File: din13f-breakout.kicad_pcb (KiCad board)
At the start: 2 copper layers, 37.8 x 42.7 mm, 5 parts, among them J1 DB15_Female_HighDensity, J2 RCJ-017, J3 Conn_01x13, J4 SDD-130J

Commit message: WIP for op-amps
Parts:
- removed J2: RCJ-017, Jacks:CUI_RCJ-017
- removed J3: Conn_01x13, Connectors:13p_GrabPads
- removed TP1: TestPoint, TestPoint:TestPoint_Pad_2.5x2.5mm
- added C1: 0.1µF, Capacitor_SMD:C_0805_2012Metric_Pad1.18x1.45mm_HandSolder, F.Cu at (163.1, 58.8)
- added C2: 0.1µF, Capacitor_SMD:C_0805_2012Metric_Pad1.18x1.45mm_HandSolder, F.Cu at (163.1, 61.8)
- added C3: 0.1µF, Capacitor_SMD:C_0805_2012Metric_Pad1.18x1.45mm_HandSolder, F.Cu at (163.1, 64.8)
- added C4: 220µF, Capacitor_THT:CP_Radial_D8.0mm_P3.50mm, F.Cu at (154.2, 62.0)
- added D1: LED, LED_THT:LED_D3.0mm, F.Cu at (119.8, 64.2)
- added JP1: Jumper_2_Open, Resistor_SMD:R_0805_2012Metric_Pad1.20x1.40mm_HandSolder, F.Cu at (170.4, 40.7)
- added JP2: Jumper_2_Bridged, Jumper:SolderJumper-2_P1.3mm_Bridged_RoundedPad1.0x1.5mm, F.Cu at (170.2, 55.7)
- added JP3: Jumper_2_Bridged, Jumper:SolderJumper-2_P1.3mm_Bridged_RoundedPad1.0x1.5mm, F.Cu at (170.2, 59.3)
- added JP4: Jumper_2_Bridged, Jumper:SolderJumper-2_P1.3mm_Bridged_RoundedPad1.0x1.5mm, F.Cu at (170.2, 62.8)
- added R1: 680kΩ, Resistor_SMD:R_0805_2012Metric_Pad1.20x1.40mm_HandSolder, F.Cu at (170.4, 43.6)
- added R10: 4.3kΩ, Resistor_SMD:R_0805_2012Metric_Pad1.20x1.40mm_HandSolder, F.Cu at (179.9, 40.7)
- added R11: 4.3kΩ, Resistor_SMD:R_0805_2012Metric_Pad1.20x1.40mm_HandSolder, F.Cu at (179.9, 43.6)
- added R12: 4.3kΩ, Resistor_SMD:R_0805_2012Metric_Pad1.20x1.40mm_HandSolder, F.Cu at (179.9, 46.6)
- added R2: 330Ω, Resistor_SMD:R_0805_2012Metric_Pad1.20x1.40mm_HandSolder, F.Cu at (170.4, 46.6)
- added R3: 330Ω, Resistor_SMD:R_0805_2012Metric_Pad1.20x1.40mm_HandSolder, F.Cu at (170.4, 49.5)
- added R4: 560Ω, Resistor_SMD:R_0805_2012Metric_Pad1.20x1.40mm_HandSolder, F.Cu at (170.4, 52.5)
- added R5: 1kΩ, Resistor_SMD:R_0805_2012Metric_Pad1.20x1.40mm_HandSolder, F.Cu at (175.1, 40.7)
- added R6: 1kΩ, Resistor_SMD:R_0805_2012Metric_Pad1.20x1.40mm_HandSolder, F.Cu at (175.1, 43.6)
- added R7: 10kΩ, Resistor_SMD:R_0805_2012Metric_Pad1.20x1.40mm_HandSolder, F.Cu at (175.1, 46.6)
- added R8: 10kΩ, Resistor_SMD:R_0805_2012Metric_Pad1.20x1.40mm_HandSolder, F.Cu at (175.1, 49.5)
- added R9: 10kΩ, Resistor_SMD:R_0805_2012Metric_Pad1.20x1.40mm_HandSolder, F.Cu at (175.1, 52.5)
- added U1: LM1881, Package_SO:SOIC-8_3.9x4.9mm_P1.27mm, F.Cu at (160.1, 123.2)
- added U2: 74LS00, Package_DIP:DIP-14_W7.62mm_Socket_LongPads, F.Cu at (159.4, 115.6)
- added U3: ~, Package_SO:SOIC-14_3.9x8.7mm_P1.27mm, F.Cu at (149.9, 111.8)
- added X1: USB-B1HSB6, USB-B1HSB6:OST_USB-B1HSB6, F.Cu at (189.9, 100.2)
- J1: value DB15_Female_HighDensity -> SCART-F; footprint Connector_TE_AMP_HD15:FIXED-1-1734530-1 -> ninigi-scart-ra:NINIGI-SCART-RA
- moved J4 67.6 mm to (197.3, 120.1), turned to 90 degrees
- moved J1 40.2 mm to (131.7, 111.9), turned to -90 degrees
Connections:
- J1 pad 1: /RED -> unconnected-(J1-P1-Pad1)
- J1 pad 10: /VGND -> unconnected-(J1-P10-Pad10)
- J1 pad 11: unconnected-(J1-Pad11) -> /SCART_Green
- J1 pad 13: /HSYNC -> GND
- J1 pad 14: /VSYNC -> unconnected-(J1-P14-Pad14)
- J1 pad 15: unconnected-(J1-Pad15) -> /SCART_Red
- J1 pad 16: (no net) -> /Blanking
- J1 pad 17: (no net) -> GND
- J1 pad 2: /GREEN -> Net-(J1-P2)
- J1 pad 3: /BLUE -> unconnected-(J1-P3-Pad3)
- J1 pad 4: unconnected-(J1-Pad4) -> GND
- J1 pad 5: /VGND -> GND
- J1 pad 6: /VGND -> Net-(J1-P6)
- J1 pad 7: /VGND -> /SCART_Blue
- J1 pad 8: /VGND -> /AV_Control
- J1 pad 9: unconnected-(J1-Pad9) -> GND
- J4 pad 12: /VSYNC -> /VSync
- J4 pad 13: /VGND -> GND
- J4 pad 2: /CVID -> Net-(JP1-B)
- J4 pad 4: /~{MONO} -> /~{MONO_EN}
- J4 pad 5: /AUDIO_IN -> unconnected-(J4-Pad5)
- J4 pad 9: /HSYNC -> /HSync
- J4 pad E1: Net-(J4-PadE1) -> GND
- J4 pad E2: Net-(J4-PadE1) -> GND
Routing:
- net /CVID: track 63.4 -> 0.00 mm, vias 2 -> 0
- net /VGND: track 59.5 -> 0.00 mm
- net /VSYNC: track 48.9 -> 0.00 mm
- net /HSYNC: track 48.4 -> 0.00 mm, vias 2 -> 0
- net /AUDIO_OUT: track 45.7 -> 0.00 mm, vias 2 -> 0
- net /BLUE: track 38.0 -> 0.00 mm, vias 2 -> 0
- net /AUDIO_IN: track 36.4 -> 0.00 mm, vias 2 -> 0
- net /GREEN: track 31.9 -> 0.00 mm, vias 1 -> 0
- net /RED: track 29.8 -> 0.00 mm, vias 1 -> 0
- net /GPO: track 28.8 -> 0.00 mm, vias 2 -> 0
- net /~{MONO}: track 27.1 -> 0.00 mm, vias 2 -> 0
- net Net-(J4-PadE1): track 19.3 -> 0.00 mm, vias 1 -> 0
- net /+12V: track 17.0 -> 0.00 mm, vias 2 -> 0
- net /MONOVID: track 12.1 -> 0.00 mm, vias 1 -> 0
- removed copper zone on B.Cu, net /VGND
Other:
- board outline removed
- board text removed: "+12V"
- board text removed: "1"
- board text removed: "13"
- board text removed: "2022, v0.1"
- board text removed: "Aud. In"
- board text removed: "Aud. Out"
- board text removed: "B"
- board text removed: "Blue"
- board text removed: "C.Video"
- board text removed: "G"
- board text removed: "GPO"
- board text removed: "Green"
- board text removed: "HS"
- board text removed: "HSync"
- board text removed: "Mono Video"
- board text removed: "R"
- board text removed: "Red"
- board text removed: "Shield GND"
- board text removed: "TE 1-1734530-1"
- board text removed: "VGA"
- board text removed: "VS"
- board text removed: "VSync"
- board text removed: "leadedsolder.com"
- board text removed: "st monitor 13-pin DIN breakout"
- board text removed: "~{MONO}"

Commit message: No more DIP
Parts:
- added C5: 0.1µF, Capacitor_SMD:C_0805_2012Metric_Pad1.18x1.45mm_HandSolder, F.Cu at (139.9, 64.1)
- U2: footprint Package_DIP:DIP-14_W7.62mm_Socket_LongPads -> Package_SO:SOIC-14_3.9x8.7mm_P1.27mm
- U3: value ~ -> MCP6499
- moved U3 10.3 mm to (140.4, 108.0)
- moved U2 2.60 mm to (160.0, 113.0), turned to 0 degrees

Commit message: Laying out the birdseed
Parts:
- moved R3 88.5 mm to (143.9, 134.0)
- moved R2 88.3 mm to (143.8, 130.8)
- moved R1 81.1 mm to (172.1, 124.7), turned to -90 degrees
- moved R11 80.0 mm to (144.3, 115.3)
- moved JP1 79.0 mm to (177.4, 119.4)
- moved JP3 77.8 mm to (139.7, 130.8)
- moved JP4 77.4 mm to (139.7, 134.0)
- moved R8 73.8 mm to (139.7, 114.3), turned to 90 degrees
- moved R12 70.3 mm to (152.4, 111.3)
- moved JP2 70.0 mm to (149.2, 122.6)
- moved R6 70.0 mm to (145.8, 107.2), turned to -90 degrees
- moved R10 68.3 mm to (152.4, 103.1)
- moved R5 67.0 mm to (157.0, 105.1), turned to -90 degrees
- moved R9 65.8 mm to (147.8, 112.3), turned to 90 degrees
- moved C1 64.5 mm to (153.4, 122.6)
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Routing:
- net Net-(U1-VIDEO): track 0.00 -> 3.14 mm
- net /SCART_CSYNC: track 0.00 -> 2.54 mm

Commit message: Fully popped
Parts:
- added REF**: MountingHole_3.2mm_M3_DIN965_Pad, MountingHole:MountingHole_3.2mm_M3_DIN965_Pad, F.Cu at (151.8, 90.2)
- added REF**: MountingHole_3.2mm_M3_DIN965_Pad, MountingHole:MountingHole_3.2mm_M3_DIN965_Pad, F.Cu at (193.7, 90.2)
- added REF**: MountingHole_3.2mm_M3_DIN965_Pad, MountingHole:MountingHole_3.2mm_M3_DIN965_Pad, F.Cu at (151.8, 133.3)
- added REF**: MountingHole_3.2mm_M3_DIN965_Pad, MountingHole:MountingHole_3.2mm_M3_DIN965_Pad, F.Cu at (193.7, 133.3)
- added TP1: TestPoint, TestPoint:TestPoint_Loop_D2.50mm_Drill1.0mm, F.Cu at (176.5, 132.7)
- added TP2: TestPoint, TestPoint:TestPoint_Loop_D2.50mm_Drill1.0mm, F.Cu at (169.5, 132.7)
- added TP3: TestPoint, TestPoint:TestPoint_Loop_D2.50mm_Drill1.0mm, F.Cu at (136.5, 124.5)
- added TP4: TestPoint, TestPoint:TestPoint_Loop_D2.50mm_Drill1.0mm, F.Cu at (151.8, 117.5)
- moved C4 36.6 mm to (173.4, 111.4), turned to -90 degrees
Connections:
- J4 pad 9: /HSync -> /Hsync
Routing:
- net +5V: track 0.00 -> 113.3 mm, vias 0 -> 5
- net /RED: track 0.00 -> 64.0 mm, vias 0 -> 2
- net /AUDIO_OUT: track 0.00 -> 54.7 mm, vias 0 -> 2
- net /BLUE: track 0.00 -> 52.3 mm, vias 0 -> 1
- net /GREEN: track 0.00 -> 51.0 mm, vias 0 -> 1
- net GND: track 0.00 -> 50.2 mm, vias 0 -> 12
- net Net-(J1-P20): track 0.00 -> 49.2 mm, vias 0 -> 2
- net /Csync: track 0.00 -> 36.7 mm, vias 0 -> 4
- net /Hsync: track 0.00 -> 27.0 mm, vias 0 -> 1
- net /SCART_Green: track 0.00 -> 23.8 mm, vias 0 -> 2
- net /SCART_Blue: track 0.00 -> 23.4 mm, vias 0 -> 2
- net /Vsync: track 0.00 -> 17.0 mm, vias 0 -> 2
- net Net-(J1-P6): track 0.00 -> 16.3 mm
- net Net-(U3D-D+): track 0.00 -> 15.3 mm
- net Net-(J1-P2): track 0.00 -> 14.5 mm
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- added copper zone on B.Cu, net GND
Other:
- board outline added: 76.8 x 55.9 mm
- board text added: "5v"
- board text added: "JLCJLCJLCJLC"
- board text added: "SCART"
- board text added: "TP3 = Green In TP4 = Green Amp."
- board text added: "gnd"
- board text added: "to Atari SC1224 CRT leadedsolder.com 2024 v1.0"

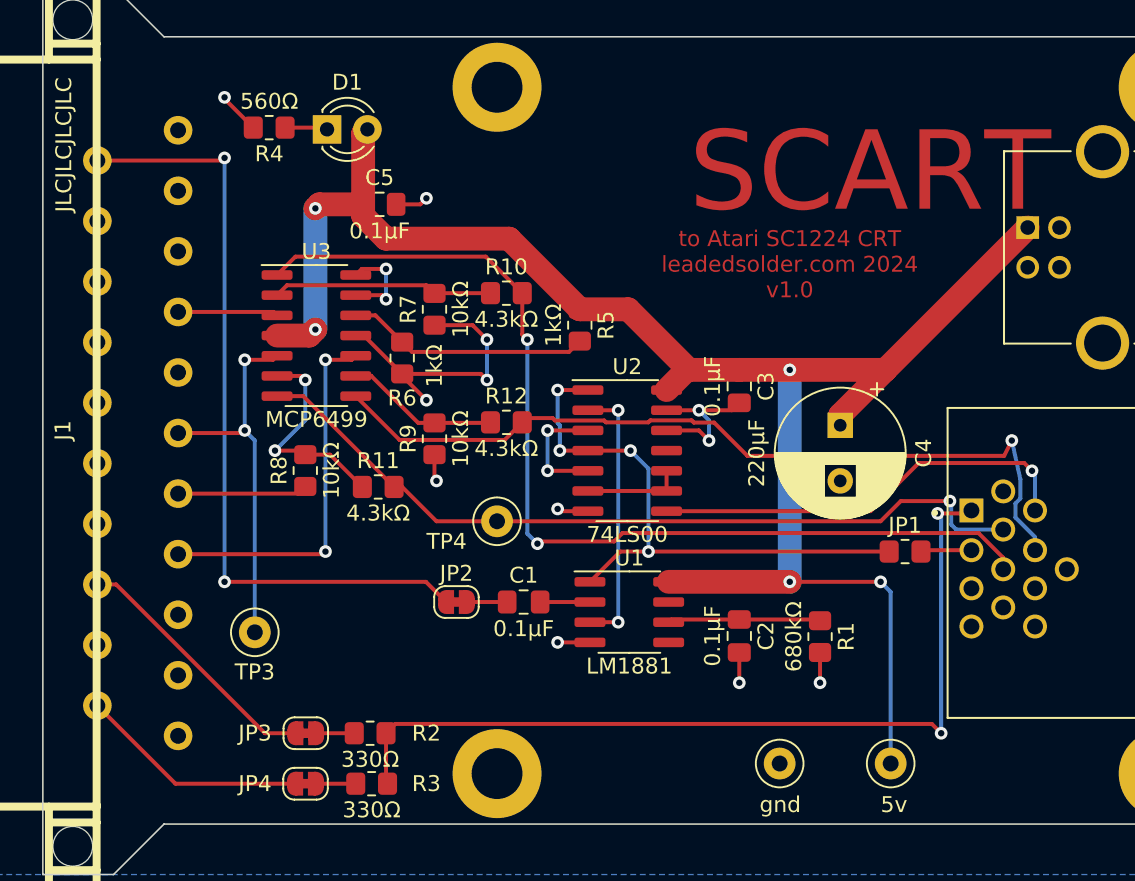
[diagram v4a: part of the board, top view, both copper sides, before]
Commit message: Rounded tracks
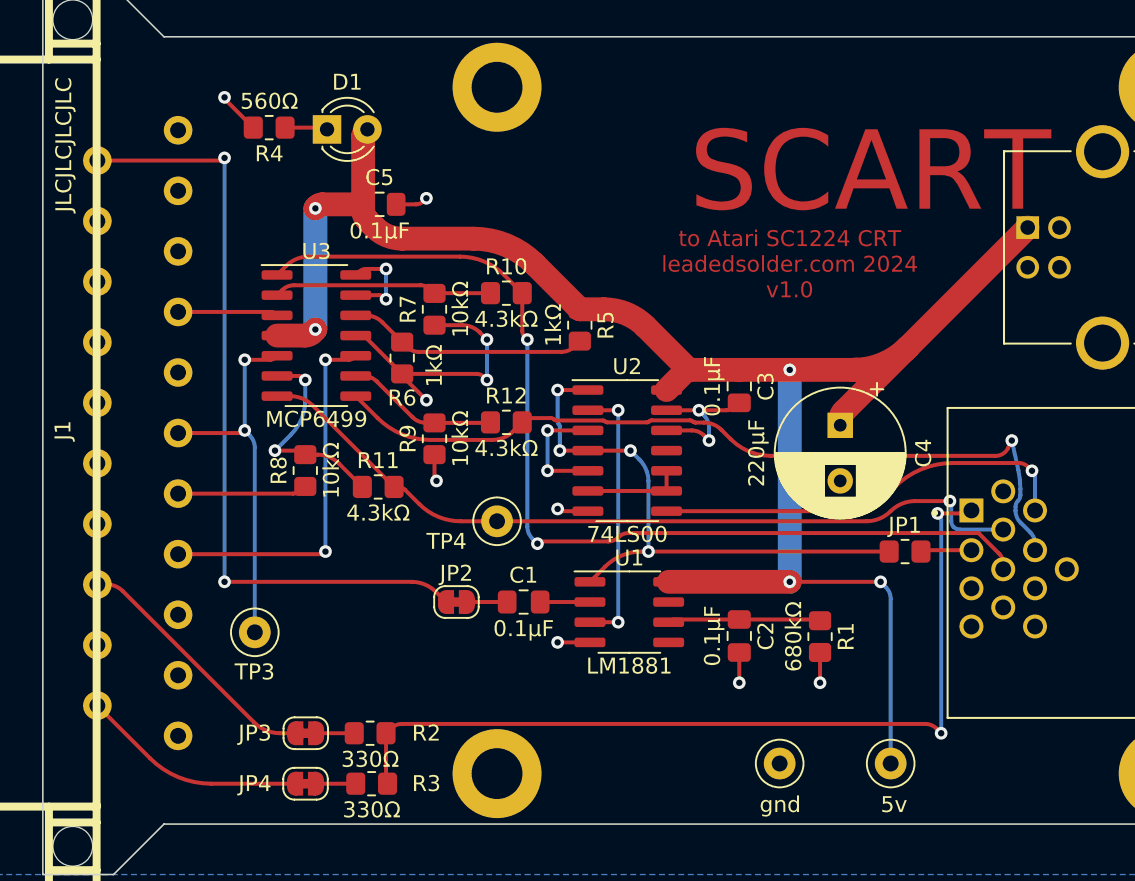
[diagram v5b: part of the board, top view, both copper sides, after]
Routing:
- net +5V: track 113.3 -> 116.9 mm
- net /BLUE: track 52.3 -> 51.3 mm
- net /GREEN: track 51.0 -> 50.4 mm
- net /Hsync: track 27.0 -> 26.5 mm
- net /RED: track 64.0 -> 63.5 mm

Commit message: Fix missing Vsync
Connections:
- J4 pad 12: /VSync -> /Vsync
- REF** pad 1: (no net) -> GND (x4)
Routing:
- net /Vsync: track 17.0 -> 44.7 mm
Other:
- board text added: "12v?"
- board text added: "Audio"
- board text added: "Blue"
- board text added: "GND"
- board text added: "Hs"
- board text added: "Vs"
